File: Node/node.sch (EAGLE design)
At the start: 33 parts, among them SW1 SWITCH-MOMENTARY-2PTH, SW2 SWITCH-MOMENTARY-2PTH, SW3 SWITCH-MOMENTARY-2PTH, U1 FT232RLSSOP, U2 DW1000-I, U4 ATMEGA328, X2 332-02, Y1 8MHz

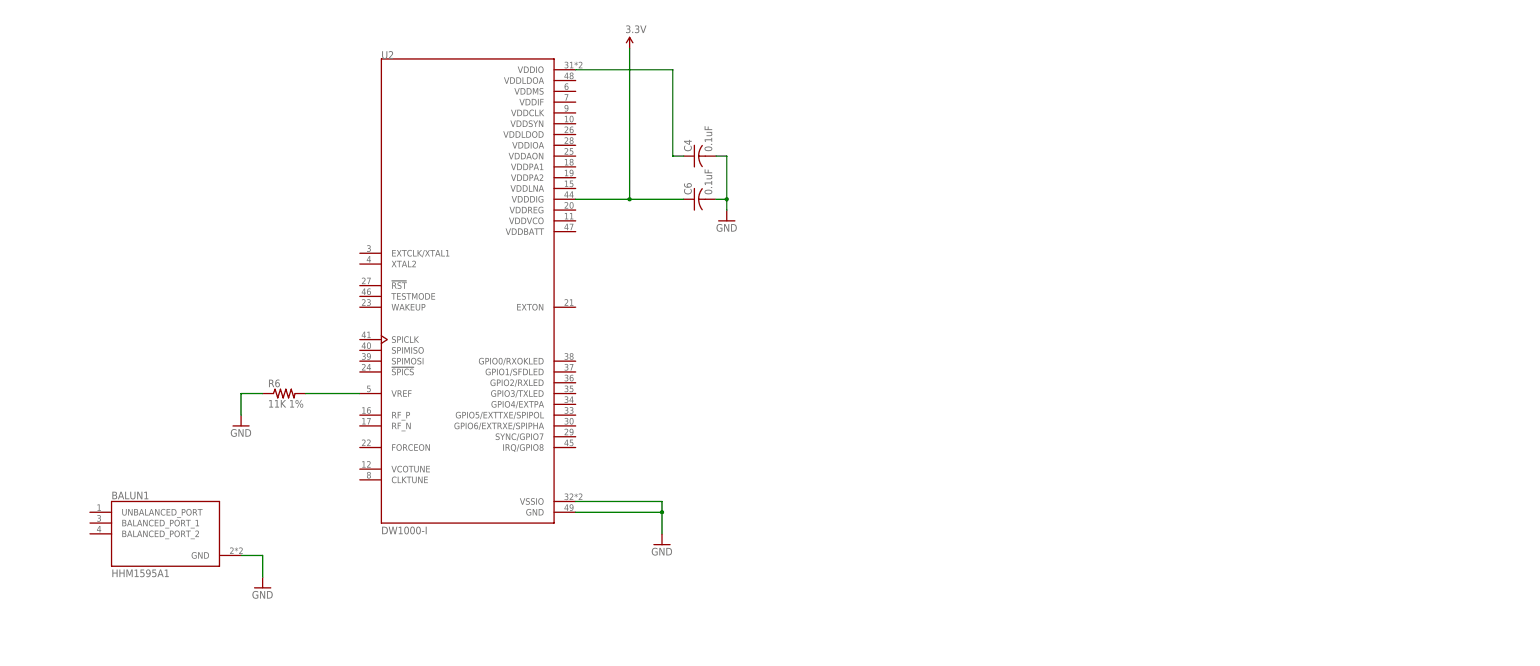
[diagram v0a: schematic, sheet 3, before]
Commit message: Work on the DW1000 SCH
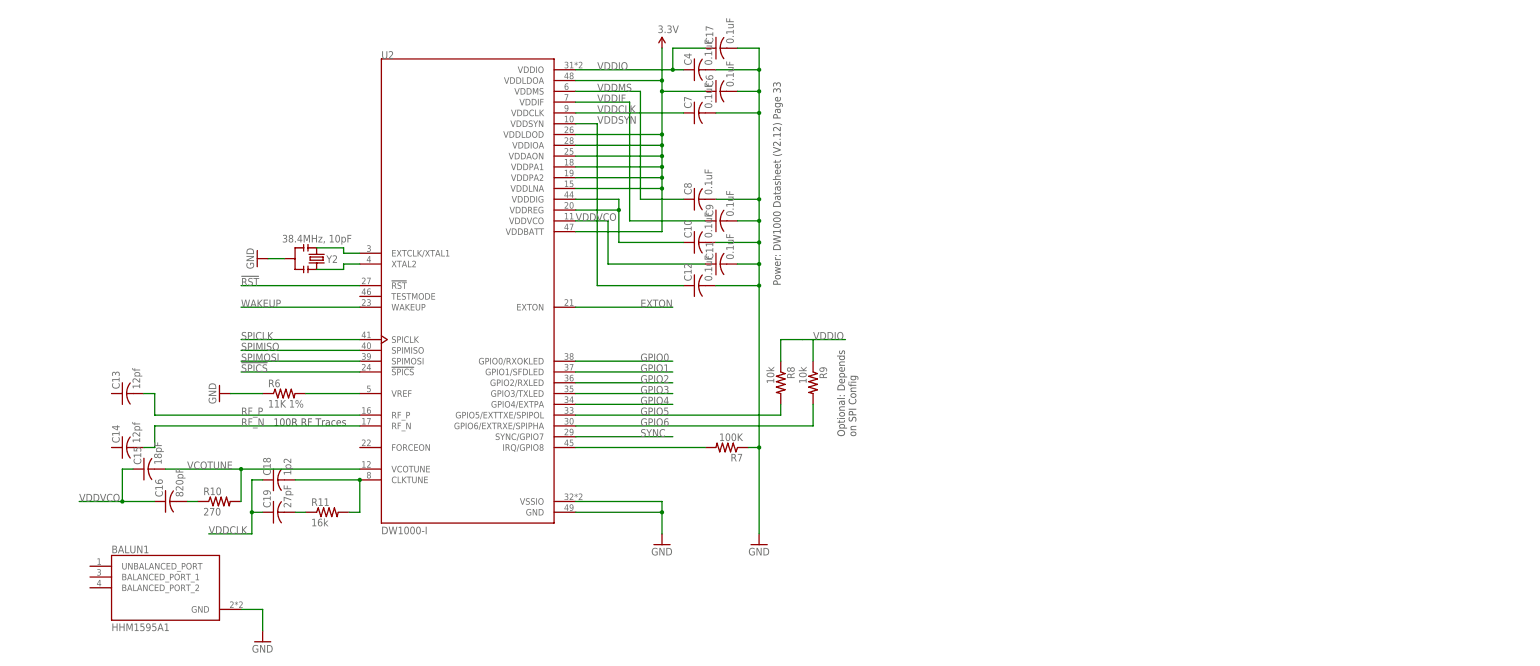
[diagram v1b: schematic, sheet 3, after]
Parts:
- added C10, C11, C12, C17, C7, C8, C9: 0.1uF, adafruit:C-USC0603K
- added C13, C14: 12pf, adafruit:C-USC0603K
- added C15: 18pF, adafruit:C-USC0603K
- added C16: 820pF, adafruit:C-USC0603K
- added C18: 1p2, adafruit:C-USC0603K
- added C19: 27pF, adafruit:C-USC0603K
- added R10: 270, SparkFun-Resistors:RESISTOR0603-RES
- added R11: 16k, SparkFun-Resistors:RESISTOR0603-RES
- added R7: 100K, SparkFun-Resistors:RESISTOR0603-RES
- added R8, R9: 10k, SparkFun-Resistors:RESISTOR0603-RES
- added Y2: 38.4MHz, 10pF, SparkFun-FreqCtrl:RESONATORSMD
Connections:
- new net !RST: U2.!RST
- new net !SPICS: U2.!SPICS
- new net EXTON: U2.EXTON
- new net GPIO0: U2.GPIO0/RXOKLED
- new net GPIO1: U2.GPIO1/SFDLED
- new net GPIO2: U2.GPIO2/RXLED
- new net GPIO3: U2.GPIO3/TXLED
- new net GPIO4: U2.GPIO4/EXTPA
- new net GPIO5: R8.2, U2.GPIO5/EXTTXE/SPIPOL
- new net GPIO6: R9.2, U2.GPIO6/EXTRXE/SPIPHA
- new net N$10: C10.1, U2.VDDDIG, U2.VDDREG
- new net N$11: C18.2, R11.2, U2.CLKTUNE
- new net N$12: U2.XTAL2, Y2.3
- new net N$13: U2.EXTCLK/XTAL1, Y2.1
- new net N$14: C19.2, R11.1
- new net N$16: R7.2, U2.IRQ/GPIO8
- new net RF_N: C14.2, U2.RF_N
- new net RF_P: C13.2, U2.RF_P
- new net SPICLK: U2.SPICLK
- new net SPIMISO: U2.SPIMISO
- new net SPIMOSI: U2.SPIMOSI
- new net SYNC: U2.SYNC/GPIO7
- new net VCOTUNE: C15.2, R10.2, U2.VCOTUNE
- new net VDDCLK: C18.1, C19.1, C7.1, U2.VDDCLK
- new net VDDIF: C9.1, U2.VDDIF
- new net VDDIO: C17.1, C4.1, R8.1, R9.1, U2.VDDIO
- new net VDDMS: C8.1, U2.VDDMS
- new net VDDSYN: C12.1, U2.VDDSYN
- new net VDDVCO: C11.1, C15.1, C16.1, U2.VDDVCO
- new net WAKEUP: U2.WAKEUP
- net 3.3V: now also U2.VDDAON, U2.VDDBATT, U2.VDDIOA, U2.VDDLDOA, U2.VDDLDOD, U2.VDDLNA, U2.VDDPA1, U2.VDDPA2; no longer U2.VDDDIG
- net GND: now also C10.2, C11.2, C12.2, C17.2, C7.2, C8.2, C9.2, R7.1, Y2.2
- net N$7: now also C16.2, R10.1; no longer C4.1, U2.VDDIO
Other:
- note added: "100R RF Traces"
- note added: "Optional: Depends on SPI Config"
- note added: "Power: DW1000 Datasheet (V2.12) Page 33"
- moved on the sheet: BALUN1, C4, C6

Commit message: Added some required ground connections
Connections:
- net GND: now also U2.FORCEON, U2.TESTMODE
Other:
- note added: "CONTAINS INTERNAL CLOCK ALSO"
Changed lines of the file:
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@@
 <part name="Y2" library="SparkFun-FreqCtrl" deviceset="RESONATOR" device="SMD" value="38.4MHz, 10pF"/>
 <part name="GND11" library="SparkFun-Aesthetics" deviceset="GND" device=""/>
+<part name="GND14" library="SparkFun-Aesthetics" deviceset="GND" device=""/>
+<part name="GND15" library="SparkFun-Aesthetics" deviceset="GND" device=""/>
 </parts>
 <sheets>
@@
 on SPI Config</text>
 <text x="73.66" y="66.04" size="1.778" layer="97">100R RF Traces</text>
+<text x="71.12" y="111.76" size="1.778" layer="97">CONTAINS INTERNAL
+CLOCK ALSO</text>
 </plain>
 <instances>
@@
 <instance part="GND11" gate="1" x="69.85" y="105.41" smashed="yes" rot="R270">
 <attribute name="VALUE" x="67.31" y="107.95" size="1.778" layer="96" rot="R270"/>
+</instance>
+<instance part="GND14" gate="1" x="81.28" y="96.52" smashed="yes" rot="R270">
+<attribute name="VALUE" x="78.74" y="99.06" size="1.778" layer="96" rot="R270"/>
+</instance>
+<instance part="GND15" gate="1" x="81.28" y="60.96" smashed="yes" rot="R270">
+<attribute name="VALUE" x="78.74" y="63.5" size="1.778" layer="96" rot="R270"/>
 </instance>
 </instances>
@@
 <pinref part="GND11" gate="1" pin="GND"/>
 </segment>
-</net>
+<segment>
+<pinref part="U2" gate="G$1" pin="TESTMODE"/>
+<wire x1="93.98" y1="96.52" x2="83.82" y2="96.52" width="0.1524" layer="91"/>
+<pinref part="GND14" gate="1" pin="GND"/>
+</segment>
+<segment>
+<pinref part="U2" gate="G$1" pin="FORCEON"/>
+<pinref part="GND15" gate="1" pin="GND"/>
+<wire x1="93.98" y1="60.96" x2="83.82" y2="60.96" width="0.1524" layer="91"/>
+</segment>
+</net>

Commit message: More work on schematic, documentation, frame, shielding, etc.
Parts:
- added C20: 0.1uF, SparkFun-Passives:CAP0603-CAP
- added C20-VDDLNA: 10nF, SparkFun-Passives:CAP0603-CAP
- added J1: U.FL, SparkFun-Connectors:U.FL
- added S1: WE-SHC_36103305, Wurth_Elektronik_Passive_rev15e:WE-SHC_36103305
- added TP1, TP2, TP3-OTP: TEST-POINT3X4, SparkFun-Passives:TEST-POINT3X4
- C10, C11, C12, C13, C14, C15, C16, C17, C18, C19, C4, C6, C7, C8, C9: device adafruit:C-USC0603K -> SparkFun-Passives:CAP0603-CAP
- Y1: value 8MHz -> 4MHz; device SparkFun-FreqCtrl:RESONATORSMD -> SparkFun-FreqCtrl:RESONATOR4MHZ
- Y2: value 38.4MHz, 10pF -> 4MHz; device SparkFun-FreqCtrl:RESONATORSMD -> SparkFun-FreqCtrl:RESONATOR4MHZ
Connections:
- new net ANT: BALUN1.UNBALANCED_PORT, J1.SIGNAL
- new net BAL_3: BALUN1.BALANCED_PORT_1, C14.1
- new net BAL_4: BALUN1.BALANCED_PORT_2, C13.1
- net 3.3V: now also C20-VDDLNA.1
- net GND: now also C20-VDDLNA.2, C20.1, S1.GND
- net GPIO5: now also TP1.1
- net GPIO6: now also TP2.1
- net VDDIO: now also C20.2, TP3-OTP.1
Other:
- note added: "100 Ω"
- note added: "50 Ω"
- note added: "Controlled Impedance: (JLC7628) RF trace - 100 Ω differential referenced to inner layer 1. 2 x 50 Ω single-ended RF trace can also be used. Need to ensure the traces are referenced to correct ground layer RF trace – 50 Ω single ended referenced to inner layer 1"
- note added: "DESIGN NOTE: Use test point for high voltage OTP programming Vmin 3.7V Vmax 3.9V"
- note added: "Optional"
- note added: "VDDPA1 & VDDPA2 Need Work"
- note removed: "100R RF Traces"
- note removed: "CONTAINS INTERNAL CLOCK ALSO"
- moved on the sheet: BALUN1, C10, C11, C12, C13, C14, C15, C16, C17, C18, C19, C4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

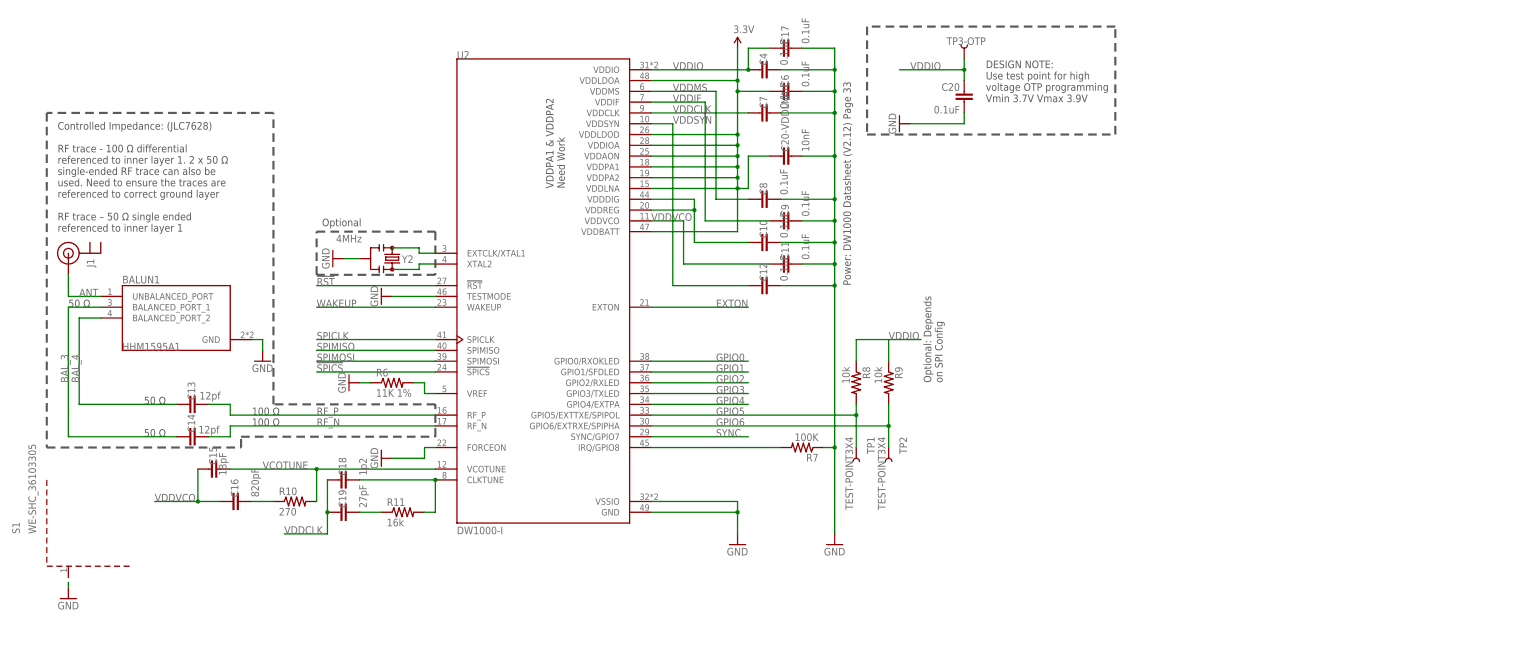
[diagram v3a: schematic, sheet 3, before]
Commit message: Moved the RF components to an area that will be covered by the RF shield. Also went through two sources and confirmed SCH and BRD layout for the DW1000 (specifically with respect to caps and resistors). Also Added the correct IO to and from the ATMEGA
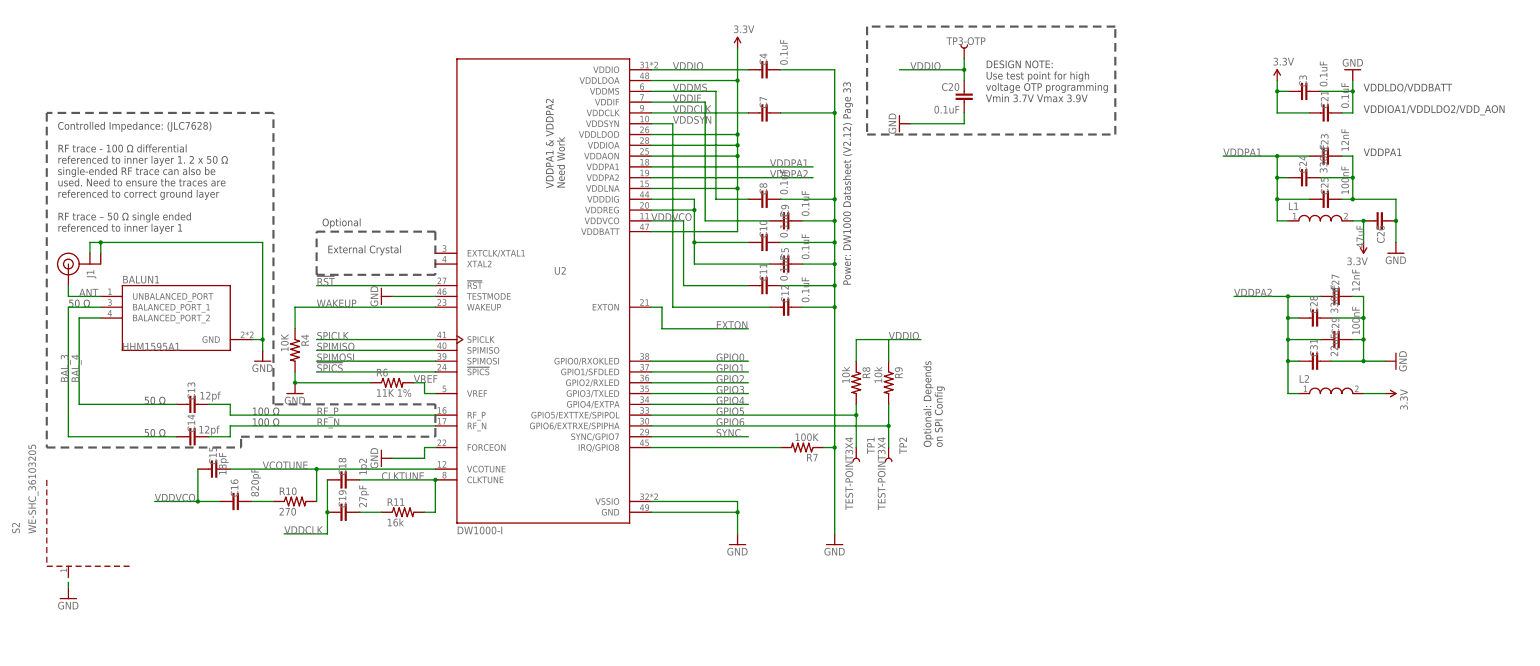
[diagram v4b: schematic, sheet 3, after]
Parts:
- removed C17, C6: 0.1uF, SparkFun-Passives:CAP0603-CAP
- removed C20-VDDLNA: 10nF, SparkFun-Passives:CAP0603-CAP
- removed R5: 150, resistor:R-US_R0805
- removed RX: R, adafruit:LEDCHIP-LED0805
- removed S1: WE-SHC_36103305, Wurth_Elektronik_Passive_rev15e:WE-SHC_36103305
- removed TX: G, adafruit:LEDCHIP-LED0805
- removed U$4: USB-MINIB-5PIN, SparkFun-Connectors:USB-MINIB-5PIN
- removed U1: FT232RLSSOP, SparkFun:FT232RLSSOP
- removed Y2: 4MHz, SparkFun-FreqCtrl:RESONATOR4MHZ
- added C21: 0.1uF, SparkFun-Passives:CAP0402-CAP
- added C23, C27: 12nF, SparkFun-Passives:CAP0402-CAP
- added C24, C28: 330nF, SparkFun-Passives:CAP0402-CAP
- added C25, C29: 100nF, SparkFun-Passives:CAP0402-CAP
- added C26: 47uF, SparkFun-Passives:CAP0402-CAP
- added C31: 22uF, SparkFun-Passives:CAP0402-CAP
- added L1, L2: BLM15AG601SN1D, Wurth_Elektronik_Passive_rev15e:WE-CBA_0402(HC)
- added S2: WE-SHC_36103205, Wurth_Elektronik_Passive_rev15e:WE-SHC_36103205
- added SJ1, SJ2, SJ3: SOLDERJUMPERTRACE, SparkFun-Retired:SOLDERJUMPERTRACE
- C10, C11, C12, C13, C14, C15, C16, C18, C19, C20, C4, C7, C8, C9: device SparkFun-Passives:CAP0603-CAP -> SparkFun-Passives:CAP0402-CAP
- C3, C5: value 1.0uF -> 0.1uF; device SparkFun-Capacitors:1.0UF-25V-+80/-20(0805)" -> SparkFun-Passives:CAP0402-CAP
- R1, R2, R3: value 150 -> 100
- R10, R11, R6, R7, R8, R9: device SparkFun-Resistors:RESISTOR0603-RES -> SparkFun-Passives:RESISTOR0402-RES
- R4: value 150 -> 10K; device resistor:R-US_R0805 -> SparkFun-Passives:RESISTOR0402-RES
- Y1: value 4MHz -> 8MHz
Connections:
- net A_ALT renamed D7
- net A_SPD renamed A6
- net B_ALT renamed D8
- net B_SPD renamed A7
- net N$11 renamed CLKTUNE
- net N$8 renamed VREF
- net SCL renamed A5
- net SDA renamed A4
- net SW1 renamed A3
- net SW3 renamed D10
- net S_ALT renamed A2
- net S_HDG renamed A1
- removed net 5V: 5.TP, C3.1, FTDI.3, RST.2, RX.A, TX.A, U$4.VBUS, U1.VCC, U1.VCCIO, U4.AVCC, U4.VCC@1, U4.VCC@2
- removed net A_HDG: U4.PD4(XCK/T0)
- removed net B_HDG: U4.PD5(T1)
- removed net IO13: S.TP, U4.PB5(SCK)
- removed net N$12: U2.XTAL2, Y2.3
- removed net N$13: U2.EXTCLK/XTAL1, Y2.1
- removed net N$5: R5.2, RX.C
- removed net N$6: R4.2, TX.C
- removed net RXI: FTDI.5, U1.RXD, U4.PD1(TXD)
- removed net RXLED: R5.1, U1.RXLED
- removed net S-RX: I.TP, U4.PB4(MISO)
- removed net S-TX: O.TP, U4.PB3(MOSI/OC2)
- removed net SW2: SW2.2, U4.PD2(INT0)
- removed net S_SPD: U4.PC0(ADC0)
- removed net TXLED: R4.1, U1.TXLED
- removed net TXO: FTDI.4, U1.TXD, U4.PD0(RXD)
- removed net USB_D+: U$4.D+, U1.USBDP
- removed net USB_D-: U$4.D-, U1.USBDM
- new net D2: SW2.2
- new net MISO: I.TP, SJ2.1, U4.PB4(MISO)
- new net MOSI: O.TP, SJ3.1, U4.PB3(MOSI/OC2)
- new net RXD: FTDI.4, U4.PD0(RXD)
- new net SCK: S.TP, SJ1.1, U4.PB5(SCK)
- new net TXD: FTDI.5, U4.PD1(TXD)
- new net VDDPA1: C23.1, C24.1, C25.1, L1.1, U2.VDDPA1
- new net VDDPA2: C27.1, C28.1, C29.1, C31.1, L2.1, U2.VDDPA2
- net !RST: now also U4.PD4(XCK/T0)
- net !SPICS: now also U4.PD2(INT0)
- net 3.3V: now also 5.TP, C21.1, C26.2, C3.1, FTDI.3, L1.2, L2.2, RST.2, U4.AVCC, U4.VCC@1, U4.VCC@2; no longer C20-VDDLNA.1, C5.1, C6.1, U1.3V3OUT, U2.VDDPA1, U2.VDDPA2
- net DTR: no longer U1.DTR
- net EXTON: now also U4.PC0(ADC0)
- net GND: now also C21.2, C23.2, C24.2, C25.2, C26.1, C27.2, C28.2, C29.2, C31.2, J1.GND@0, J1.GND@1, R4.2, S2.GND; no longer C17.2, C20-VDDLNA.2, C6.2, S1.GND, U$4.GND, U$4.MTN1, U$4.MTN2, U$4.MTN3, U$4.MTN4, U1.AGND, U1.GND18, U1.GND21, U1.GND7, U1.TEST, Y2.2
- net N$10: now also C5.1
- net SPICLK: now also SJ1.2
- net SPIMISO: now also SJ2.2
- net SPIMOSI: now also SJ3.2
- net VDDIO: no longer C17.1
- net WAKEUP: now also R4.1, U4.PD5(T1)
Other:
- note added: "External Crystal"
- note added: "VDDIOA1/VDDLDO2/VDD_AON"
- note added: "VDDLDO/VDDBATT"
- note added: "VDDPA1"
- moved on the sheet: C11, C12, C2, J1

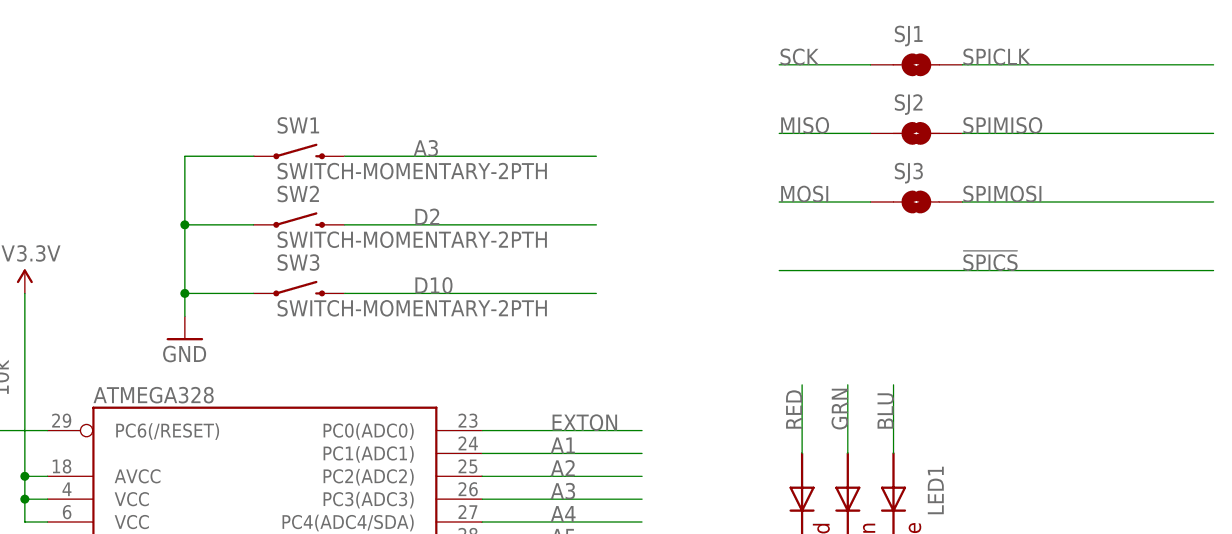
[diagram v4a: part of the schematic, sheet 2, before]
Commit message: Added the RF Shield to the sch and brd, then routed all components of the current schematic
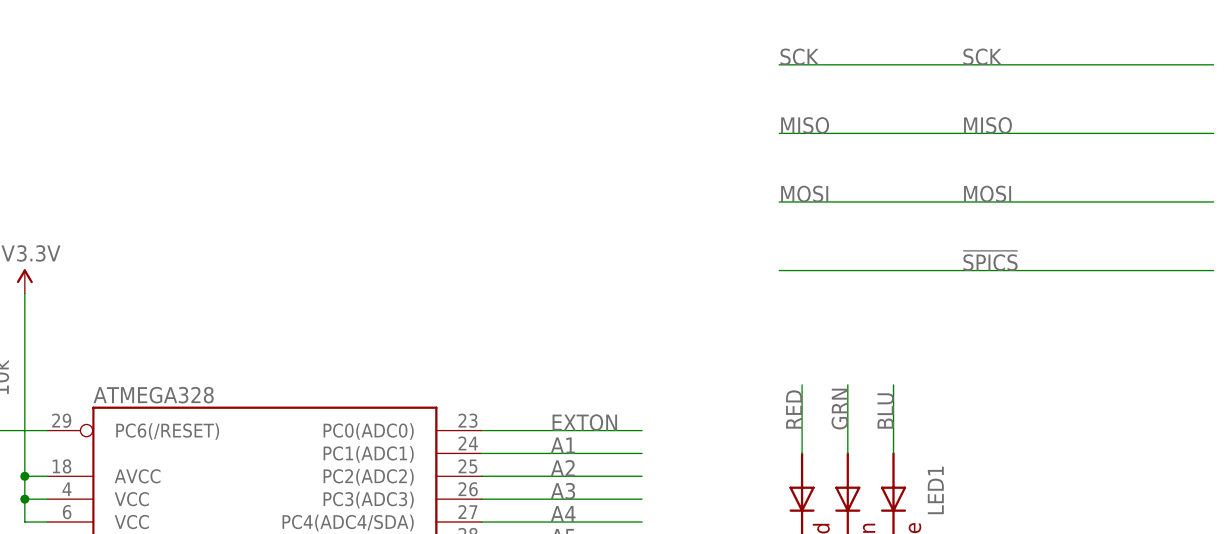
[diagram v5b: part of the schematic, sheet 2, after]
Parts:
- removed S2: WE-SHC_36103205, Wurth_Elektronik_Passive_rev15e:WE-SHC_36103205
- removed SJ1, SJ2, SJ3: SOLDERJUMPERTRACE, SparkFun-Retired:SOLDERJUMPERTRACE
- removed SW1, SW2, SW3: SWITCH-MOMENTARY-2PTH, SparkFun-Electromechanical:SWITCH-MOMENTARY-2PTH
- added U$1: 5BMI-S-202-F, MainLib:5BMI-S-202-F
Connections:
- net BAL_3 renamed BAL_N
- net BAL_4 renamed BAL_P
- removed net D2: SW2.2
- removed net SPICLK: SJ1.2, U2.SPICLK
- removed net SPIMISO: SJ2.2, U2.SPIMISO
- removed net SPIMOSI: SJ3.2, U2.SPIMOSI
- net A3: no longer SW1.2
- net D10: no longer SW3.2
- net GND: now also U$1.P$1; no longer S2.GND, SW1.1, SW2.1, SW3.1
- net MISO: now also U2.SPIMISO; no longer SJ2.1
- net MOSI: now also U2.SPIMOSI; no longer SJ3.1
- net SCK: now also U2.SPICLK; no longer SJ1.1
